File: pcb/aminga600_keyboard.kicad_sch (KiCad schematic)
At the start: 21 parts

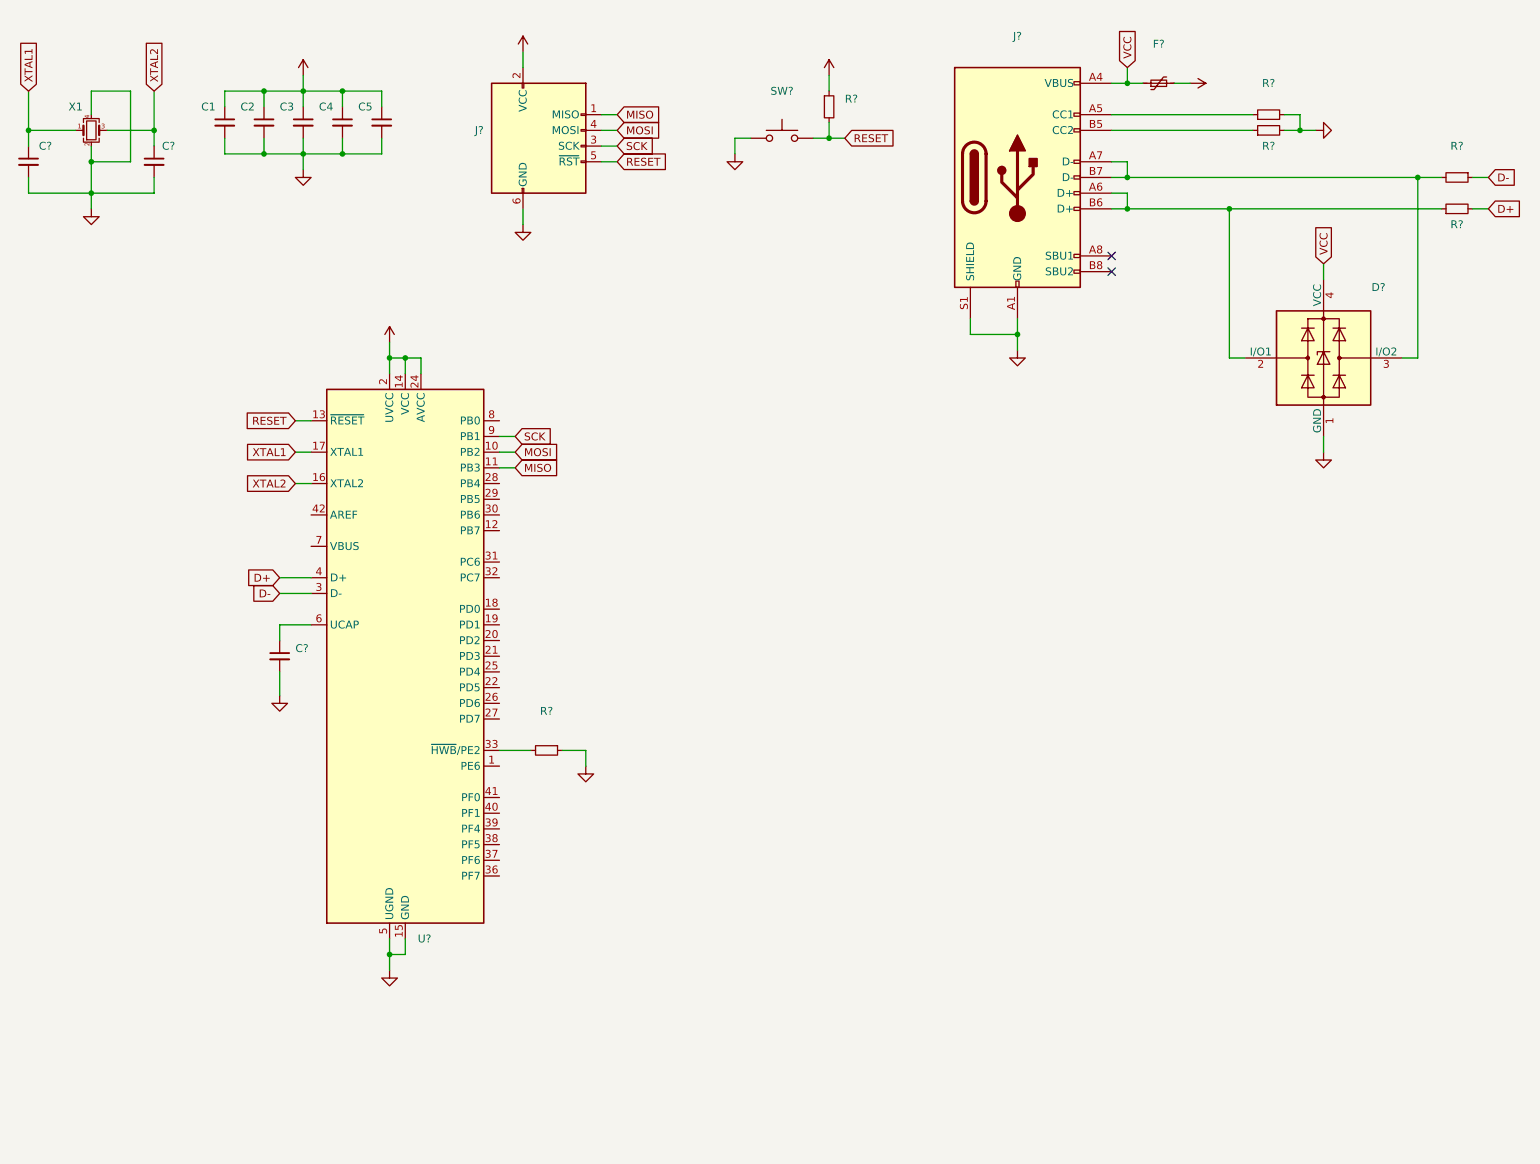
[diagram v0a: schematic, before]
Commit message: Schematics done, pcb in the work.
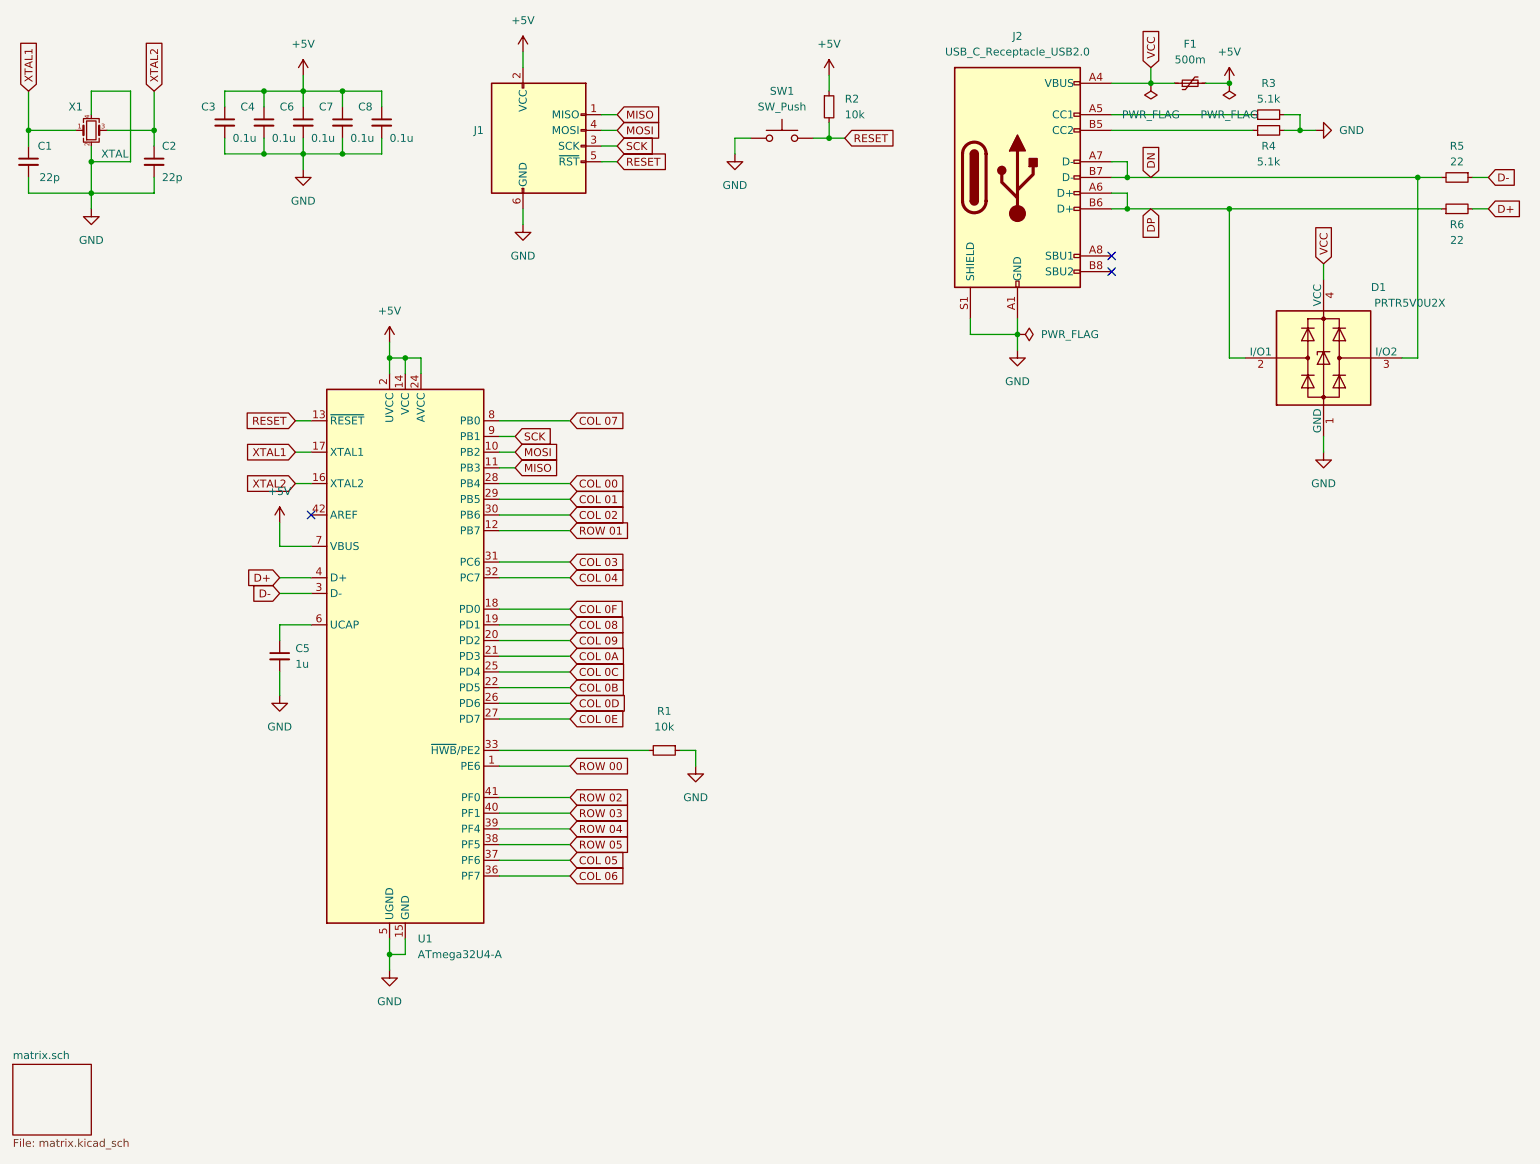
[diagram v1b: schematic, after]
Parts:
- C1, C2: renamed from C?; value (none) -> 22p; footprint (none) -> Diode_SMD:D_0805_2012Metric_Pad1.15x1.40mm_HandSolder
- C3: renamed from C1; value (none) -> 0.1u; footprint (none) -> Diode_SMD:D_0805_2012Metric_Pad1.15x1.40mm_HandSolder
- C4: renamed from C2; value (none) -> 0.1u; footprint (none) -> Diode_SMD:D_0805_2012Metric_Pad1.15x1.40mm_HandSolder
- C5: renamed from C?; value (none) -> 1u; footprint (none) -> Diode_SMD:D_0805_2012Metric_Pad1.15x1.40mm_HandSolder
- C6: renamed from C3; value (none) -> 0.1u; footprint (none) -> Diode_SMD:D_0805_2012Metric_Pad1.15x1.40mm_HandSolder
- C7: renamed from C4; value (none) -> 0.1u; footprint (none) -> Diode_SMD:D_0805_2012Metric_Pad1.15x1.40mm_HandSolder
- C8: renamed from C5; value (none) -> 0.1u; footprint (none) -> Diode_SMD:D_0805_2012Metric_Pad1.15x1.40mm_HandSolder
- D1: renamed from D?; value (none) -> PRTR5V0U2X; footprint (none) -> Package_TO_SOT_SMD:SOT-143
- F1: renamed from F?; value (none) -> 500m; footprint (none) -> Fuse:Fuse_1206_3216Metric_Pad1.42x1.75mm_HandSolder
- J2: renamed from J?; value (none) -> USB_C_Receptacle_USB2.0; footprint (none) -> Connector_USB:USB_C_Receptacle_HRO_TYPE-C-31-M-12
- R1, R2: renamed from R?; value (none) -> 10k; footprint (none) -> Resistor_SMD:R_0805_2012Metric_Pad1.20x1.40mm_HandSolder
- R3, R4: renamed from R?; value (none) -> 5.1k; footprint (none) -> Resistor_SMD:R_0805_2012Metric_Pad1.20x1.40mm_HandSolder
- R5, R6: renamed from R?; value (none) -> 22; footprint (none) -> Resistor_SMD:R_0805_2012Metric_Pad1.20x1.40mm_HandSolder
- SW1: renamed from SW?; value (none) -> SW_Push; footprint (none) -> Button_Switch_SMD:SW_SPST_SKQG_WithoutStem
- U1: renamed from U?; value (none) -> ATmega32U4-A; footprint (none) -> Package_QFP:TQFP-44_10x10mm_P0.8mm
- X1: value (none) -> XTAL; footprint (none) -> Crystal:Crystal_SMD_3225-4Pin_3.2x2.5mm_HandSoldering
- gave numbers to parts that had none: 1
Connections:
- net +5V: now also U1.7 (VBUS)
- net DN: now reaches D1.3 (I/O2), J2.A7 (D-), J2.B7 (D-), R5.2
- net DP: now reaches D1.2 (I/O1), J2.A6 (D+), J2.B6 (D+), R6.1
- net ROW 00: now reaches U1.1 (PE6)
- net ROW 01: now reaches U1.12 (PB7)
- net COL 0F: now reaches U1.18 (PD0)
- net COL 08: now reaches U1.19 (PD1)
- net COL 09: now reaches U1.20 (PD2)
- net COL 0A: now reaches U1.21 (PD3)
- net COL 0B: now reaches U1.22 (PD5)
- net COL 0C: now reaches U1.25 (PD4)
- net COL 0D: now reaches U1.26 (PD6)
- net COL 0E: now reaches U1.27 (PD7)
- net COL 00: now reaches U1.28 (PB4)
- net COL 01: now reaches U1.29 (PB5)
- net COL 02: now reaches U1.30 (PB6)
- net COL 03: now reaches U1.31 (PC6)
- net COL 04: now reaches U1.32 (PC7)
- net COL 06: now reaches U1.36 (PF7)
- net COL 05: now reaches U1.37 (PF6)
- net ROW 05: now reaches U1.38 (PF5)
- net ROW 04: now reaches U1.39 (PF4)
- net ROW 03: now reaches U1.40 (PF1)
- net ROW 02: now reaches U1.41 (PF0)
- net COL 07: now reaches U1.8 (PB0)
- no-connect marks 2 -> 3
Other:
- added sheet matrix.sch (matrix.kicad_sch)
- moved on the sheet: F1, R1
